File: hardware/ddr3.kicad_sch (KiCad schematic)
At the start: 7 parts, among them U2 H5TQ4G63EFR

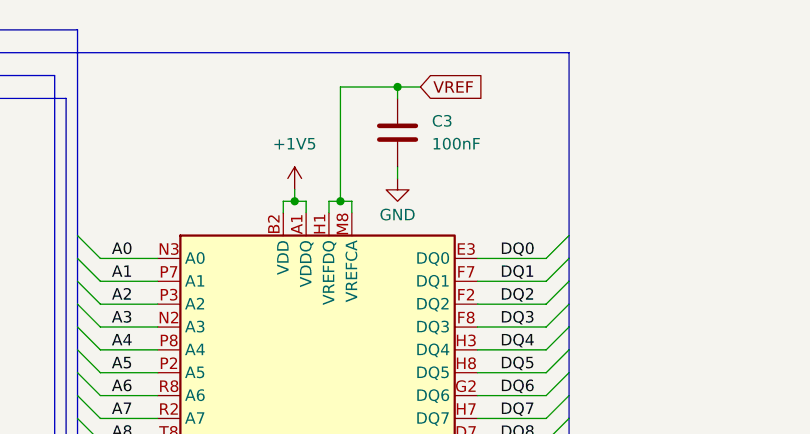
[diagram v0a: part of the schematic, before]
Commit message: Re-routed DDR3 on L4 & drew USB schematic
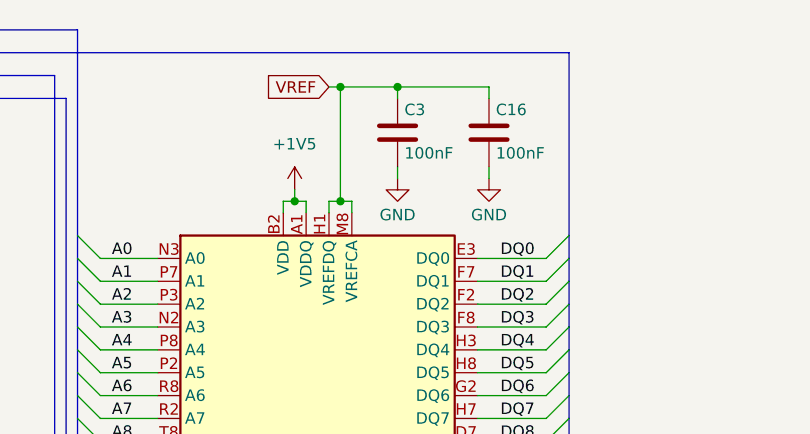
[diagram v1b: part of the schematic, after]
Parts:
- added C16: 100nF, Capacitor_SMD:C_0402_1005Metric, symbol Device:C
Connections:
- net GND: now also C16.2
- net VREF: now also C16.1
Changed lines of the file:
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@@
 	)
 	(junction
+		(at 83.82 35.56)
+		(diameter 0)
+		(color 0 0 0 0)
+	)
+	(junction
 		(at 144.78 68.58)
 		(diameter 0)
@@
 	(wire
 		(pts
+			(xy 100.33 35.56) (xy 100.33 36.83)
+		)
+		(stroke
+			(width 0)
+			(type default)
+		)
+	)
+	(wire
+		(pts
 			(xy 99.06 59.69) (xy 106.68 59.69)
 		)
@@
 	(wire
 		(pts
+			(xy 82.55 35.56) (xy 83.82 35.56)
+		)
+		(stroke
+			(width 0)
+			(type default)
+		)
+	)
+	(wire
+		(pts
 			(xy 99.06 100.33) (xy 106.68 100.33)
 		)
@@
 		)
 	)
+	(wire
+		(pts
+			(xy 100.33 44.45) (xy 100.33 45.72)
+		)
+		(stroke
+			(width 0)
+			(type default)
+		)
+	)
 	(bus
 		(pts
@@
 	(wire
 		(pts
-			(xy 90.17 35.56) (xy 92.71 35.56)
+			(xy 90.17 35.56) (xy 100.33 35.56)
 		)
 		(stroke
@@
 	(global_label "VREF"
 		(shape input)
-		(at 92.71 35.56 0)
+		(at 82.55 35.56 180)
 		(fields_autoplaced yes)
 		(effects
@@
 				(size 1.27 1.27)
 			)
-			(justify left)
+			(justify right)
 		)
 		(property "Intersheetrefs" "${INTERSHEET_REFS}"
-			(at 100.2914 35.56 0)
+			(at 74.9686 35.56 0)
 			(effects
 				(font
 					(size 1.27 1.27)
 				)
-				(justify left)
+				(justify right)
 				(hide yes)
 			)
@@
 	)
 	(symbol
+		(lib_id "Device:C")
+		(at 100.33 40.64 0)
+		(unit 1)
+		(exclude_from_sim no)
+		(in_bom yes)
+		(on_board yes)
+		(dnp no)
+		(property "Reference" "C16"
+			(at 101.092 38.1 0)
+			(effects
+				(font
+					(size 1.27 1.27)
+				)
+				(justify left)
+			)
+		)
+		(property "Value" "100nF"
+			(at 101.092 42.926 0)
+			(effects
+				(font
+					(size 1.27 1.27)
+				)
+				(justify left)
+			)
+		)
+		(property "Footprint" "Capacitor_SMD:C_0402_1005Metric"
+			(at 101.2952 44.45 0)
+			(effects
+				(font
+					(size 1.27 1.27)
+				)
+				(hide yes)
+			)
+		)
+		(property "Datasheet" "~"
+			(at 100.33 40.64 0)
+			(effects
+				(font
+					(size 1.27 1.27)
+				)
+				(hide yes)
+			)
+		)
+		(property "Description" "Unpolarized capacitor"
+			(at 100.33 40.64 0)
+			(effects
+				(font
+					(size 1.27 1.27)
+				)
+				(hide yes)
+			)
+		)
+		(property "LCSC Part #" ""
+			(at 100.33 40.64 0)
+			(effects
+				(font
+					(size 1.27 1.27)
+				)
+				(hide yes)
+			)
+		)
+		(pin "2"
+		)
+		(pin "1"
+		)
+		(instances
+			(project "cm0"
+				(path "/b53f5dbb-8078-4818-9e8f-fdf90ba6d854/32a4bb18-2695-4537-bbd4-f872ec13cb53"
+					(reference "C16")
+					(unit 1)
+				)
+			)
+		)
+	)
+	(symbol
 		(lib_id "Device:R")
 		(at 140.97 53.34 0)
@@
 	)
 	(symbol
+		(lib_id "power:GND")
+		(at 100.33 45.72 0)
+		(unit 1)
+		(exclude_from_sim no)
+		(in_bom yes)
+		(on_board yes)
+		(dnp no)
+		(property "Reference" "#PWR034"
+			(at 100.33 52.07 0)
+			(effects
+				(font
+					(size 1.27 1.27)
+				)
+				(hide yes)
+			)
+		)
+		(property "Value" "GND"
+			(at 100.33 49.784 0)
+			(effects
+				(font
+					(size 1.27 1.27)
+				)
+			)
+		)
+		(property "Footprint" ""
+			(at 100.33 45.72 0)
+			(effects
+				(font
+					(size 1.27 1.27)
+				)
+				(hide yes)
+			)
+		)
+		(property "Datasheet" ""
+			(at 100.33 45.72 0)
+			(effects
+				(font
+					(size 1.27 1.27)
+				)
+				(hide yes)
+			)
+		)
+		(property "Description" "Power symbol creates a global label with name \"GND\" , ground"
+			(at 100.33 45.72 0)
+			(effects
+				(font
+					(size 1.27 1.27)
+				)
+				(hide yes)
+			)
+		)
+		(pin "1"
+		)
+		(instances
+			(project "cm0"
+				(path "/b53f5dbb-8078-4818-9e8f-fdf90ba6d854/32a4bb18-2695-4537-bbd4-f872ec13cb53"
+					(reference "#PWR034")
+					(unit 1)
+				)
+			)
+		)
+	)
+	(symbol
 		(lib_id "Device:C")
 		(at 148.59 53.34 0)
@@
 		(on_board yes)
 		(dnp no)
-		(fields_autoplaced yes)
 		(property "Reference" "C3"
-			(at 93.98 39.3699 0)
+			(at 90.932 38.1 0)
 			(effects
 				(font
@@
 		)
 		(property "Value" "100nF"
-			(at 93.98 41.9099 0)
+			(at 90.932 42.926 0)
 			(effects
 				(font
